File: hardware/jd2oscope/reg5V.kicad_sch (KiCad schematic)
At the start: 11 parts, among them J1 9V_CONN, U3 NCP1117-5.0_SOT223

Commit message: feat: more stuff added
yep
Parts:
- BT1: now not fitted
- J1: footprint (none) -> TerminalBlock_RND:TerminalBlock_RND_205-00001_1x02_P5.00mm_Horizontal

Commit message: feat: finished schematics
I think! Subject to change tho! for now though at least, I think they look clean asf hah~
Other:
- note added: "Decoupling Capacitor Information: 0.1u = Ceramic 10u = Electrolytic"
- note removed: "Capacitor Information: 0.1u = Ceramic 10u = Electrolytic"
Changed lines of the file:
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@@
 		)
 	)
-	(text "Capacitor Information:\n0.1u = Ceramic\n10u = Electrolytic"
+	(text "Decoupling Capacitor Information:\n0.1u = Ceramic\n10u = Electrolytic"
 		(exclude_from_sim no)
-		(at 85.09 66.294 0)
+		(at 76.962 65.532 0)
 		(effects
 			(font

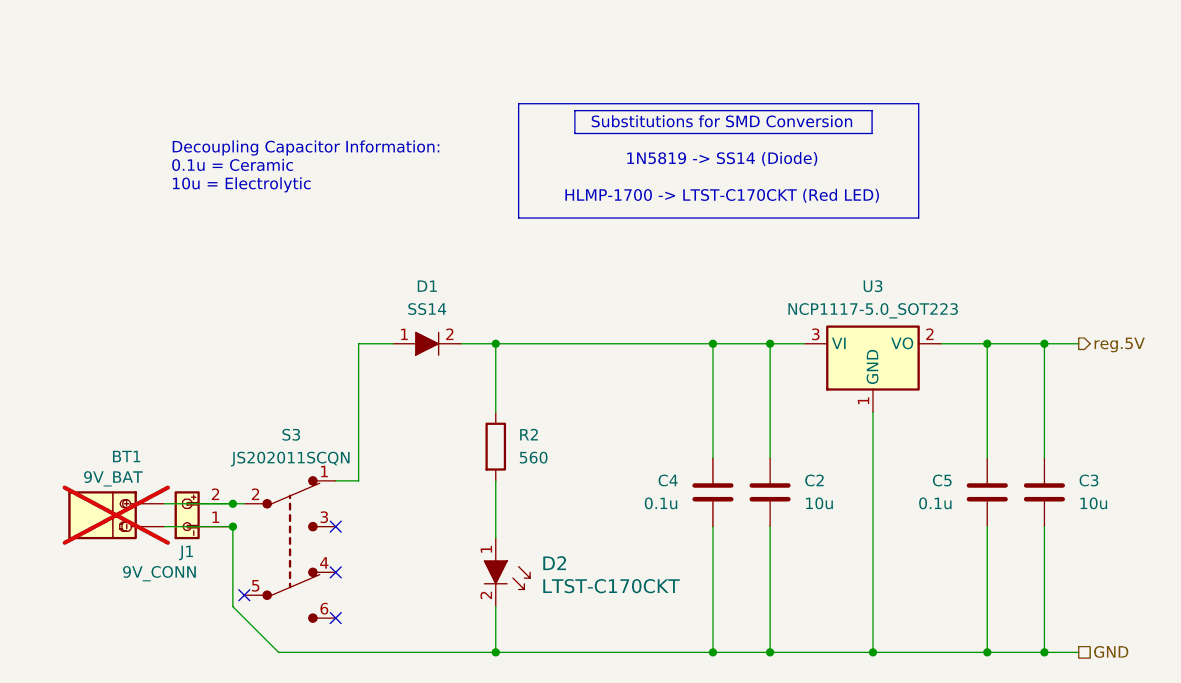
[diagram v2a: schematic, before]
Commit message: fix: ERC funtimes
fixed a bunch of dependencies with ERC checks for the schematic; shouuuuld be easier/actually possible to open on other devices now?? (added a buncha schematics & footprints to the local files & whatnot)
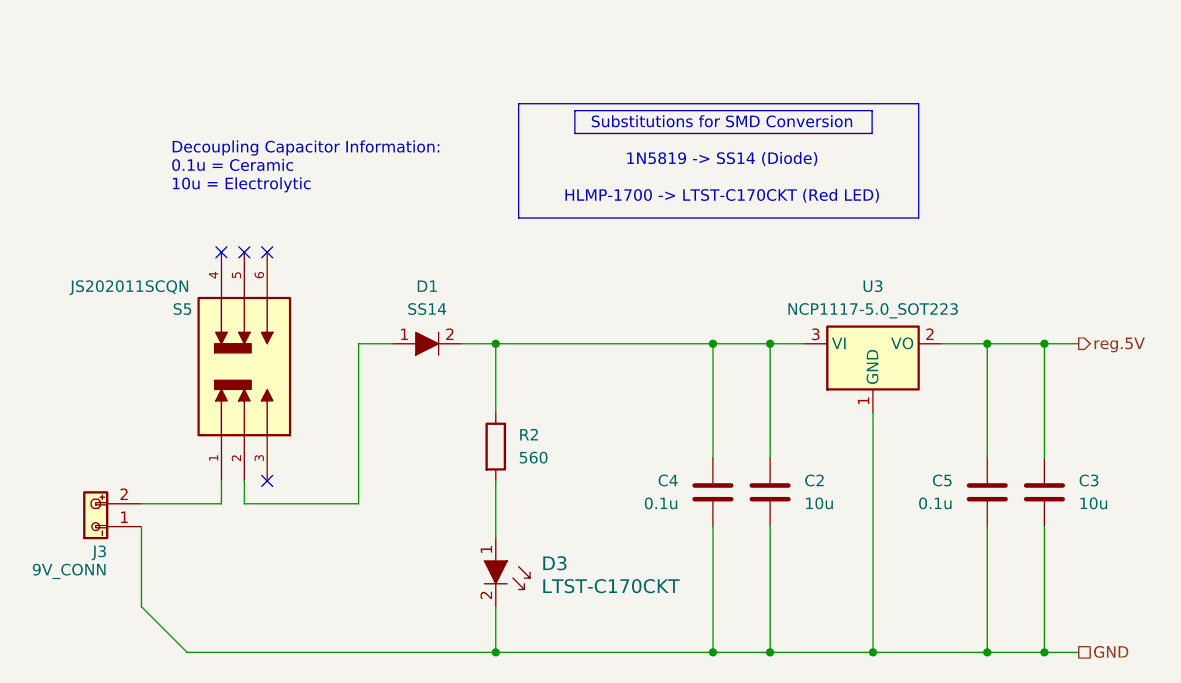
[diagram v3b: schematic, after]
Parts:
- removed BT1: 9V_BAT, symbol lockBuster:9V_BATT
- removed D1: SS14, Diode_SMD:D_SOD-123, symbol dk_Diodes-Rectifiers-Single:SS14
- removed D2: LTST-C170CKT, LED_SMD:LED_0805_2012Metric, symbol dk_LED-Indication-Discrete:LTST-C170KFKT
- removed J1: 9V_CONN, TerminalBlock_RND:TerminalBlock_RND_205-00001_1x02_P5.00mm_Horizontal, symbol lockBuster:Conn_PP3
- removed S3: JS202011SCQN, digikey-footprints:Switch_Slide_JS202011SCQN, symbol dk_Slide-Switches:JS202011SCQN
- added D1: SS14, Diode_SMD:D_SOD-123, symbol jd2Oscope_diodes:SS14
- added D3: LTST-C170CKT, LED_SMD:LED_0805_2012Metric, symbol jd2Oscope_diodes:LTST-C170KFKT
- added J3: 9V_CONN, TerminalBlock_RND:TerminalBlock_RND_205-00001_1x02_P5.00mm_Horizontal, symbol 9VBatteryComponents:Conn_PP3_1
- added S5: JS202011SCQN, JS202011SCQN:SW_JS202011SCQN, symbol JS202011SCQN:JS202011SCQN
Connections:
- net GND: now also D3.2, J3.1 (Pin_1)
- net at C2.1, C4.2, R2.1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: now also D1.2
- net at R2.2: now also D3.1
- new net: J3.2 (Pin_2), S5.1
- new net: D1.1, S5.2

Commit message: feat/fix: no more errors for PCB import too!
Now both the ERC, and the schematic import (and my OCD) are completely satisfied, and we can dev the actual PCB; let's go!! :D
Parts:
- S1: renamed from S5; footprint JS202011SCQN:SW_JS202011SCQN -> jd2Oscope_Footprints:SW_JS202011SCQN
- renumbered C2 to C5, C5 to C6, C3 to C7, D3 to D2, J3 to J1
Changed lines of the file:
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@@
 		(on_board yes)
 		(dnp no)
-		(property "Reference" "C5"
+		(property "Reference" "C6"
 			(at 163.83 100.3299 0)
 			(effects
@@
 			(project "jd2oscope"
 				(path "/eb18a3da-9fbf-4329-a814-1afab785c817/d124c55c-b59b-4d66-8527-4d5db5a79d29"
-					(reference "C5")
+					(reference "C6")
 					(unit 1)
 				)
@@
 		(on_board yes)
 		(dnp no)
-		(property "Reference" "J3"
+		(property "Reference" "J1"
 			(at 69.85 108.204 90)
 			(effects
@@
 			(project ""
 				(path "/eb18a3da-9fbf-4329-a814-1afab785c817/d124c55c-b59b-4d66-8527-4d5db5a79d29"
-					(reference "J3")
+					(reference "J1")
 					(unit 1)
 				)
@@
 		(dnp no)
 		(fields_autoplaced yes)
-		(property "Reference" "C3"
+		(property "Reference" "C7"
 			(at 177.8 100.3299 0)
 			(effects
@@
 			(project "jd2oscope"
 				(path "/eb18a3da-9fbf-4329-a814-1afab785c817/d124c55c-b59b-4d66-8527-4d5db5a79d29"
-					(reference "C3")
+					(reference "C7")
 					(unit 1)
 				)
@@
 		(dnp no)
 		(fields_autoplaced yes)
-		(property "Reference" "D3"
+		(property "Reference" "D2"
 			(at 118.11 109.5374 90)
 			(effects
@@
 			(project ""
 				(path "/eb18a3da-9fbf-4329-a814-1afab785c817/d124c55c-b59b-4d66-8527-4d5db5a79d29"
-					(reference "D3")
+					(reference "D2")
 					(unit 1)
 				)
@@
 		(dnp no)
 		(fields_autoplaced yes)
-		(property "Reference" "C2"
+		(property "Reference" "C5"
 			(at 147.32 100.3299 0)
 			(effects
@@
 			(project "jd2oscope"
 				(path "/eb18a3da-9fbf-4329-a814-1afab785c817/d124c55c-b59b-4d66-8527-4d5db5a79d29"
-					(reference "C2")
+					(reference "C5")
 					(unit 1)
 				)
@@
 		(on_board yes)
 		(dnp no)
-		(property "Reference" "S5"
+		(property "Reference" "S1"
 			(at 78.232 81.28 90)
 			(effects
@@
 			)
 		)
-		(property "Footprint" "JS202011SCQN:SW_JS202011SCQN"
+		(property "Footprint" "jd2Oscope_Footprints:SW_JS202011SCQN"
 			(at 85.09 87.63 0)
 			(effects
@@
 			(project ""
 				(path "/eb18a3da-9fbf-4329-a814-1afab785c817/d124c55c-b59b-4d66-8527-4d5db5a79d29"
-					(reference "S5")
+					(reference "S1")
 					(unit 1)
 				)

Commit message: feat:net lists & net classes implemented
labeled e/a net w/ net labels to clarify nodes, & created net classes w/ desired dimensions for traces; next up is assigning net classes to e/a net & using it to create the pcb!
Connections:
- net 9V_PwrSwitch: now reaches J1.2 (Pin_2), S1.1
- net Schottky_LEDres-caps-5Vreg.In: now reaches C4.2, C5.1, D1.2, R2.1, U3.3 (VI)
- net LEDres_LED: now reaches D2.1, R2.2
- net PwrSwitch_Schottky: now reaches D1.1, S1.2
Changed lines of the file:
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@@
+		)
+	)
+	(label "PwrSwitch_Schottky"
+		(at 97.79 87.63 90)
+		(effects
+			(font
+				(size 1.27 1.27)
+			)
+			(justify left bottom)
+		)
+	)
+	(label "9V_PwrSwitch"
+		(at 82.55 100.33 180)
+		(effects
+			(font
+				(size 1.27 1.27)
+			)
+			(justify right bottom)
+		)
+	)
+	(label "Schottky_LEDres-caps-5Vreg.In"
+		(at 111.76 85.09 90)
+		(effects
+			(font
+				(size 1.27 1.27)
+			)
+			(justify left bottom)
+		)
+	)
+	(label "LEDres_LED"
+		(at 113.03 104.14 0)
+		(effects
+			(font
+				(size 1.27 1.27)
+			)
+			(justify left bottom)
 		)
 	)

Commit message: feat: pcb complete
ha gottem
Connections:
- net PwrSwitch_Schottky: now also D1.2; no longer D1.1
- net Schottky_LEDres-caps-5Vreg.In: now also D1.1; no longer D1.2
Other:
- moved on the sheet: D1
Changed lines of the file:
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@@
+	(wire
+		(pts
+			(xy 109.22 85.09) (xy 113.03 85.09)
+		)
+		(stroke
+			(width 0)
+			(type default)
+		)
+	)
 	(wire
 		(pts
@@
 		(pts
 			(xy 137.16 119.38) (xy 143.51 119.38)
-		)
-		(stroke
-			(width 0)
-			(type default)
-		)
-	)
-	(wire
-		(pts
-			(xy 109.22 85.09) (xy 113.03 85.09)
 		)
 		(stroke
@@
 	(symbol
 		(lib_id "jd2Oscope_diodes:SS14")
-		(at 106.68 85.09 180)
+		(at 104.14 85.09 0)
 		(unit 1)
 		(exclude_from_sim no)
@@
 		)
 		(property "Footprint" "Diode_SMD:D_SOD-123"
-			(at 101.6 90.17 0)
+			(at 109.22 80.01 0)
 			(effects
 				(font
@@
 		)
 		(property "Datasheet" "https://www.onsemi.com/pub/Collateral/SS19-D.PDF"
-			(at 101.6 92.71 0)
+			(at 109.22 77.47 0)
 			(effects
 				(font
@@
 		)
 		(property "Description" "DIODE SCHOTTKY 40V 1A SMA"
-			(at 106.68 85.09 0)
+			(at 104.14 85.09 0)
 			(effects
 				(font
@@
 		)
 		(property "Digi-Key_PN" "SS14CT-ND"
-			(at 101.6 95.25 0)
+			(at 109.22 74.93 0)
 			(effects
 				(font
@@
 		)
 		(property "MPN" "SS14"
-			(at 101.6 97.79 0)
+			(at 109.22 72.39 0)
 			(effects
 				(font
@@
 		)
 		(property "Category" "Discrete Semiconductor Products"
-			(at 101.6 100.33 0)
+			(at 109.22 69.85 0)
 			(effects
 				(font
@@
 		)
 		(property "Family" "Diodes - Rectifiers - Single"
-			(at 101.6 102.87 0)
+			(at 109.22 67.31 0)
 			(effects
 				(font
@@
 		)
 		(property "DK_Datasheet_Link" "https://www.onsemi.com/pub/Collateral/SS19-D.PDF"
-			(at 101.6 105.41 0)
+			(at 109.22 64.77 0)
 			(effects
 				(font
@@
 		)
 		(property "DK_Detail_Page" "/product-detail/en/on-semiconductor/SS14/SS14CT-ND/965729"
-			(at 101.6 107.95 0)
+			(at 109.22 62.23 0)
 			(effects
 				(font
@@
 		)
 		(property "Description_1" "DIODE SCHOTTKY 40V 1A SMA"
-			(at 101.6 110.49 0)
+			(at 109.22 59.69 0)
 			(effects
 				(font
@@
 		)
 		(property "Manufacturer" "ON Semiconductor"
-			(at 101.6 113.03 0)
+			(at 109.22 57.15 0)
 			(effects
 				(font
@@
 		)
 		(property "Status" "Active"
-			(at 101.6 115.57 0)
+			(at 109.22 54.61 0)
 			(effects
 				(font
@@
 		)
 		(property "Comment" ""
-			(at 106.68 85.09 0)
+			(at 104.14 85.09 0)
 			(effects
 				(font
@@
 		)
 		(property "EU_RoHS_Compliance" ""
-			(at 106.68 85.09 0)
+			(at 104.14 85.09 0)
 			(effects
 				(font
@@
 		)
 		(property "Number_of_Positions" ""
-			(at 106.68 85.09 0)
-			(effects
-				(font
+			(at 104.14 85.09 0)
+			(effects
+				(font
